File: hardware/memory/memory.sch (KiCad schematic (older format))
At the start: 74 parts, among them J1 Conn_Mem, J2 Conn_Power, J3 Conn_Mem_Ext, U1 74HC161, U10 74HC595, U11 74HC595, U12 74HC595, U13 74HC595, U14 74HC597, U15 74HC74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

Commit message: Added ~RESET to memory bus
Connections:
- net A24: no longer J3.26 (A30)
- net A30: now also J3.26 (A30); no longer J3.27 (A31)
- net A31: now also J3.27 (A31); no longer J3.28 (~RESET)
- net ~RESET: now also J3.28 (~RESET)
- no-connect marks 9 -> 10
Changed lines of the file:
@@
 	10250 13100 10750 13100
 Wire Wire Line
-	11700 12700 12200 12700
-Text Label 11700 12700 0    50   ~ 0
+	11700 12500 12200 12500
+Text Label 10250 13200 0    50   ~ 0
 A24
 Text Label 10250 13100 0    50   ~ 0
@@
 Wire Wire Line
 	3050 2700 3050 2850
-Text Label 11700 12500 0    50   ~ 0
+Text Label 11700 12600 0    50   ~ 0
 A31
-Text Label 11700 12600 0    50   ~ 0
+Text Label 11700 12700 0    50   ~ 0
 A30
 Wire Wire Line
-	11700 12500 12200 12500
-Wire Wire Line
-	12200 12600 11700 12600
+	11700 12600 12200 12600
+Wire Wire Line
+	12200 12700 11700 12700
 Wire Wire Line
 	12200 15200 12100 15200
@@
 	1    0    0    -1
 $EndComp
+Wire Wire Line
+	10250 13200 10750 13200
+NoConn ~ 10750 13200
+Text Label 11700 12500 0    50   ~ 0
+~RESET
 $EndSCHEMATC

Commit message: Unified footprints
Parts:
- U19, U21: footprint Package_TO_SOT_SMD:SOT-23-5 -> Package_TO_SOT_SMD:SOT-23-5_HandSoldering
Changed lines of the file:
@@
 F 0 "U19" H 3050 2717 50  0000 C CNN
 F 1 "MIC5504-3.3YM5" H 3050 2626 50  0000 C CNN
-F 2 "Package_TO_SOT_SMD:SOT-23-5" H 3050 1950 50  0001 C CNN
+F 2 "Package_TO_SOT_SMD:SOT-23-5_HandSoldering" H 3050 1950 50  0001 C CNN
 F 3 "http://ww1.microchip.com/downloads/en/DeviceDoc/MIC550X.pdf" H 2800 2600 50  0001 C CNN
 	1    3050 2350
@@
 F 0 "U21" H 10000 8925 50  0000 C CNN
 F 1 "74LVC1G38" H 10000 8834 50  0000 C CNN
-F 2 "Package_TO_SOT_SMD:SOT-23-5" H 10000 8650 50  0001 C CNN
+F 2 "Package_TO_SOT_SMD:SOT-23-5_HandSoldering" H 10000 8650 50  0001 C CNN
 F 3 "" H 10000 8650 50  0001 C CNN
 	1    10000 8600
@@
 F 0 "U21" H 14750 19550 50  0000 C CNN
 F 1 "74LVC1G38" V 14600 19550 50  0000 C CNN
-F 2 "Package_TO_SOT_SMD:SOT-23-5" H 14750 19600 50  0001 C CNN
+F 2 "Package_TO_SOT_SMD:SOT-23-5_HandSoldering" H 14750 19600 50  0001 C CNN
 F 3 "" H 14750 19600 50  0001 C CNN
 	2    14750 19550

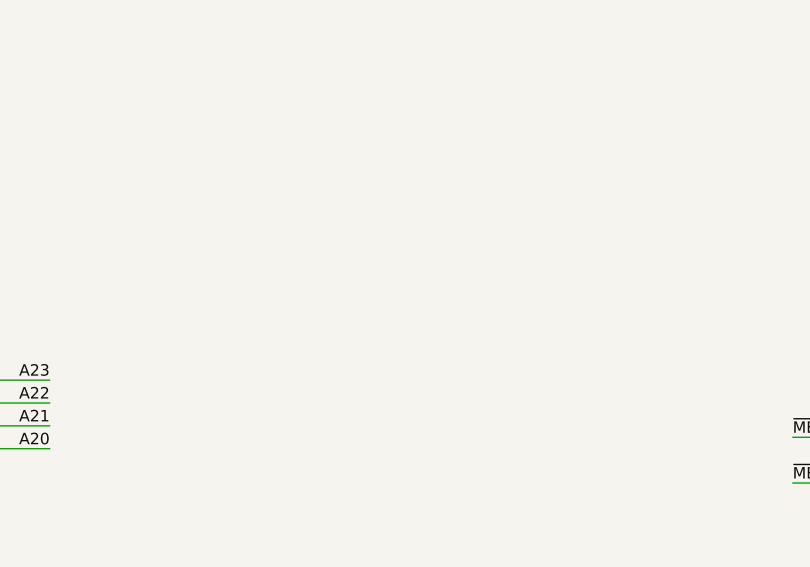
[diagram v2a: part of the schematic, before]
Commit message: Added test points
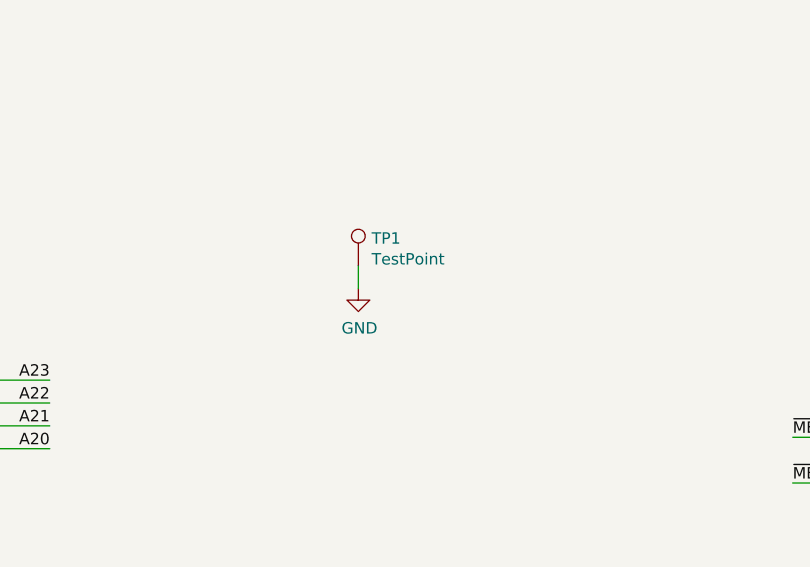
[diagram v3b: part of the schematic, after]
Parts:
- added TP1: TestPoint, TestPoint:TestPoint_THTPad_D2.0mm_Drill1.0mm, symbol Connector:TestPoint
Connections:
- net GND: now also TP1.1

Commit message: Sign bit is D7. Change 74LVC1G38 to 74LVC1G00
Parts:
- U21: value 74LVC1G38 -> 74LVC1G00; symbol riscv-serial:74LVC1G38 -> riscv-serial:74LVC1G00
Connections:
- net D0: no longer U16.1 (D)
- net D7: now also U16.1 (D)
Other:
- note added: "74LVC1G38 has open drain output\nAdd a pullup resistor or replace with 74LVC1G00"
- note added: "The sign bit is D7!"
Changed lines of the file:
@@
 EESchema Schematic File Version 4
-EELAYER 26 0
+EELAYER 30 0
 EELAYER END
 $Descr A2 16535 23386 portrait
@@
 	11600 1850 11800 1850
 Text Label 11950 1750 0    50   ~ 0
-D0
+D7
 Wire Wire Line
 	11950 1750 12150 1750
@@
 ~MEM_WE
 $Comp
-L riscv-serial:74LVC1G38 U21
+L riscv-serial:74LVC1G00 U21
 U 1 1 5EE3A29F
 P 10000 8600
 F 0 "U21" H 10000 8925 50  0000 C CNN
-F 1 "74LVC1G38" H 10000 8834 50  0000 C CNN
+F 1 "74LVC1G00" H 10000 8834 50  0000 C CNN
 F 2 "Package_TO_SOT_SMD:SOT-23-5_HandSoldering" H 10000 8650 50  0001 C CNN
 F 3 "" H 10000 8650 50  0001 C CNN
@@
 $EndComp
 $Comp
-L riscv-serial:74LVC1G38 U21
+L riscv-serial:74LVC1G00 U21
 U 2 1 5EE3BA4A
 P 14750 19550
 F 0 "U21" H 14750 19550 50  0000 C CNN
-F 1 "74LVC1G38" V 14600 19550 50  0000 C CNN
+F 1 "74LVC1G00" V 14600 19550 50  0000 C CNN
 F 2 "Package_TO_SOT_SMD:SOT-23-5_HandSoldering" H 14750 19600 50  0001 C CNN
 F 3 "" H 14750 19600 50  0001 C CNN
@@
 Wire Wire Line
 	7350 7750 7350 7850
+Text Notes 9100 9100 0    50   ~ 0
+74LVC1G38 has open drain output\nAdd a pullup resistor or replace with 74LVC1G00
+Text Notes 12000 1500 0    50   ~ 0
+The sign bit is D7!
 $EndSCHEMATC

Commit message: Fixed LED latch
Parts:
- added C23: 100n, Capacitor_SMD:C_0805_2012Metric_Pad1.18x1.45mm_HandSolder, symbol Device:C
- added U22: 74LVC1G32, Package_TO_SOT_SMD:SOT-23-5_HandSoldering, symbol riscv-serial:74LVC1G32
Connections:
- net DOUT_LATCH: now also U22.2
- net GND: now also C23.2, U22.3 (GND)
- net VCC: now also U15.1 (~R), C23.1, U22.5 (VCC); no longer U15.4 (~S)
- net ~MEM_OE: now also U22.1; no longer U21.2
- net ~RESET: now also U15.4 (~S); no longer U15.1 (~R)
- new net: U21.2, U22.4
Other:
- note removed: "74LVC1G38 has open drain output\nAdd a pullup resistor or replace with 74LVC1G00"
